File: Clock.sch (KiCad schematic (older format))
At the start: 4 parts, among them Y1 6MHz

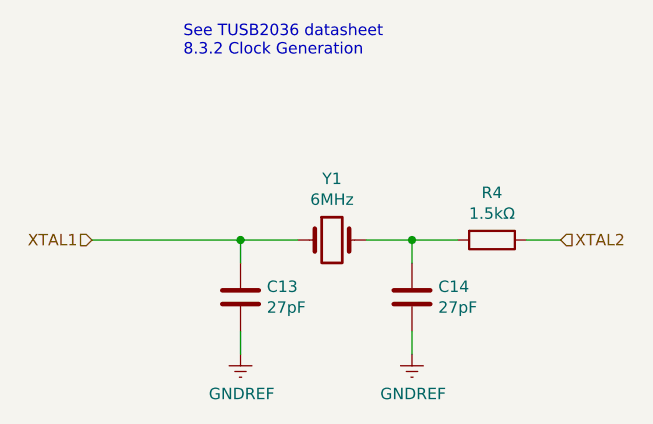
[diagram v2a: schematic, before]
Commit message: First pass at routing PCB
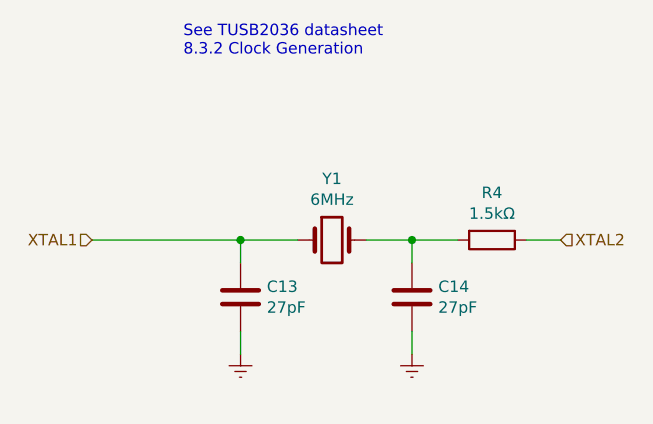
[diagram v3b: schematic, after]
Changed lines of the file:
@@
 $Descr A4 11693 8268
 encoding utf-8
-Sheet 4 6
+Sheet 3 6
 Title "TX-500 Data Interface"
 Date "2021-03-15"
 Rev "0.1"
 Comp "Chris Keller K0SWE"
-Comment1 ""
+Comment1 "Licensed under Apache-2.0"
 Comment2 ""
 Comment3 ""
@@
 P 5500 3600
 F 0 "#PWR0135" H 5500 3350 50  0001 C CNN
-F 1 "GNDREF" H 5505 3427 50  0000 C CNN
+F 1 "GNDREF" H 5505 3427 50  0001 C CNN
 F 2 "" H 5500 3600 50  0001 C CNN
 F 3 "" H 5500 3600 50  0001 C CNN
@@
 P 6250 3600
 F 0 "#PWR0136" H 6250 3350 50  0001 C CNN
-F 1 "GNDREF" H 6255 3427 50  0000 C CNN
+F 1 "GNDREF" H 6255 3427 50  0001 C CNN
 F 2 "" H 6250 3600 50  0001 C CNN
 F 3 "" H 6250 3600 50  0001 C CNN
